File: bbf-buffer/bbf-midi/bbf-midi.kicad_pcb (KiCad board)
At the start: 4 copper layers, 31.8 x 52.1 mm, 17 parts, among them J1 Conn_02x05_Odd_Even, J2 Conn_02x05_Odd_Even, J3 DIN-5_180degree, J4 DIN-5_180degree, J5 Conn_01x03, U1 TLV1117-50, U2 6N137

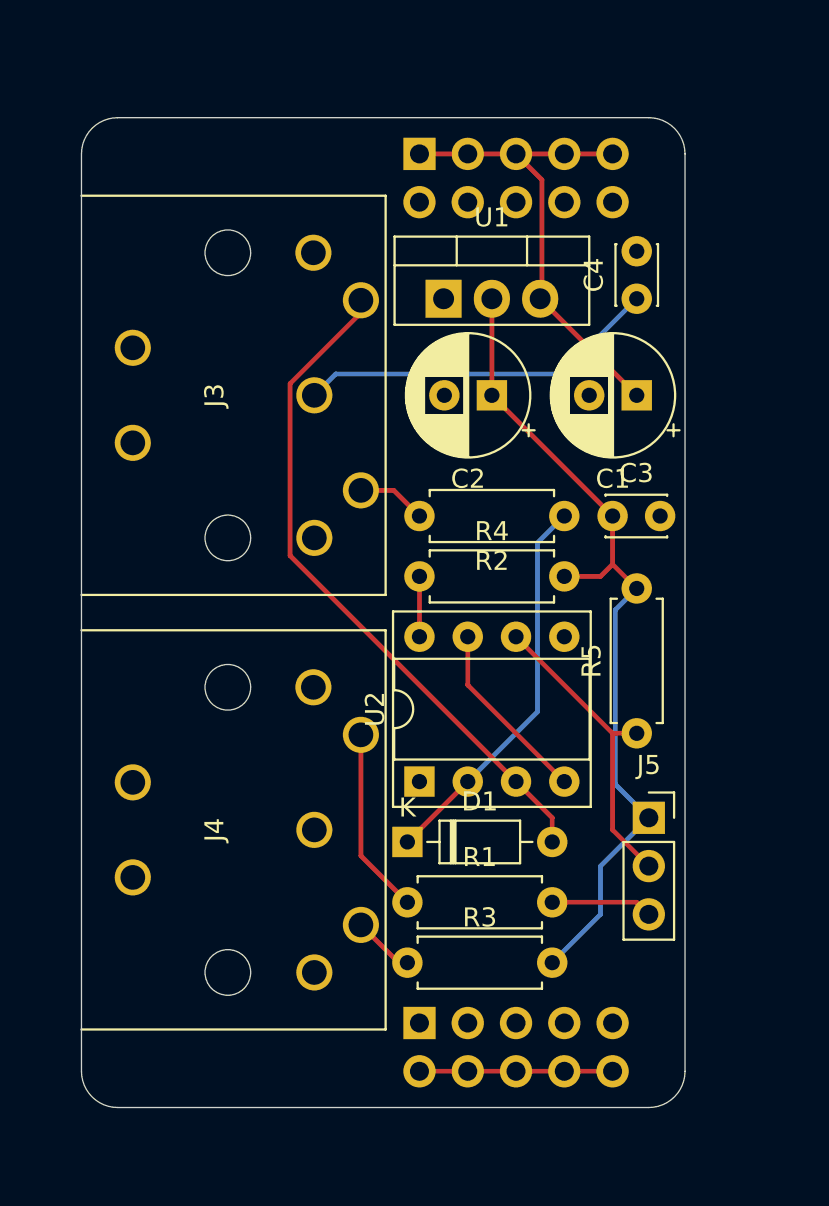
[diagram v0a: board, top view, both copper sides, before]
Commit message: Update midi friend to 3.3v, including RX buffer.
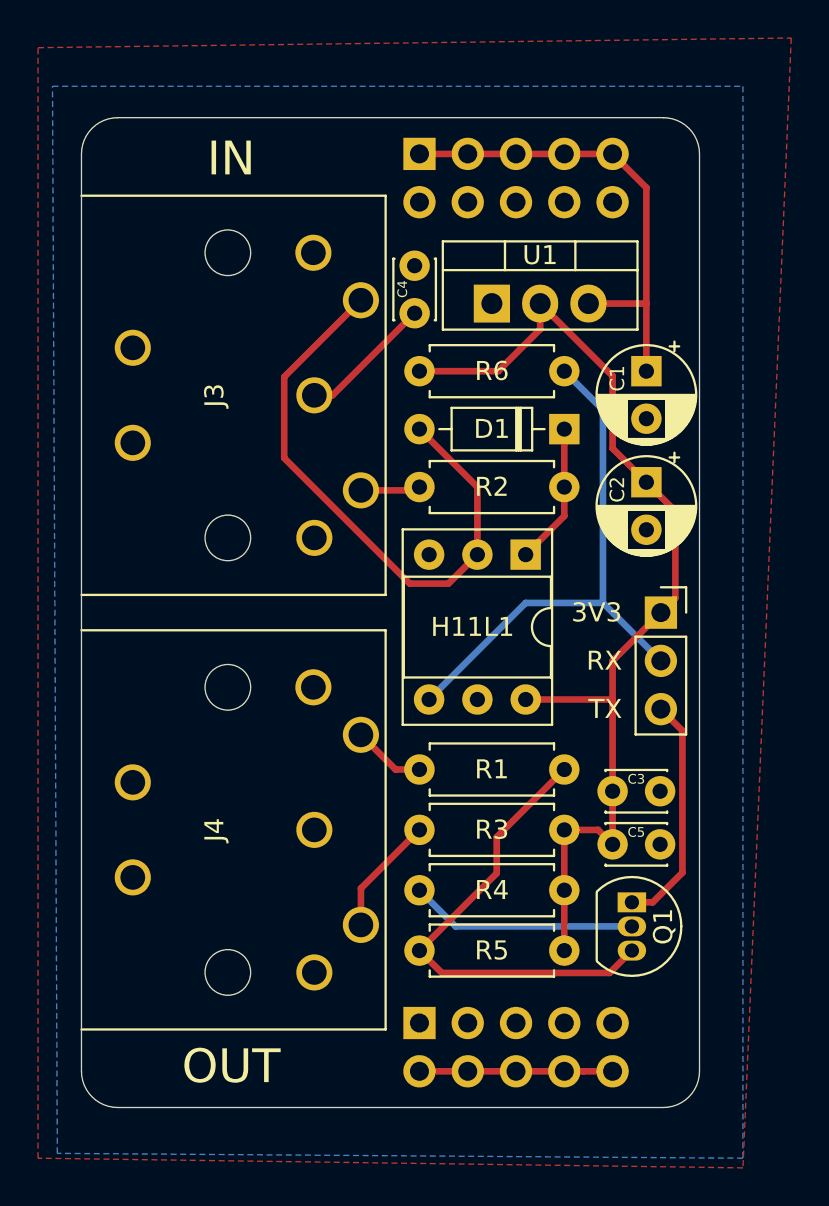
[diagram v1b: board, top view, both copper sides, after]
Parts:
- removed U2: 6N137, Package_DIP:DIP-8_W7.62mm_Socket
- added C5: 100n, Capacitor_THT:C_Disc_D3.0mm_W2.0mm_P2.50mm, F.Cu at (152.4, 125.2)
- added H11L1: H11L1, Package_DIP:DIP-6_W7.62mm_Socket, F.Cu at (147.8, 110.0)
- added Q1: 2N3904, Package_TO_SOT_THT:TO-92_Inline, F.Cu at (153.4, 128.3)
- added R5: 1K, Resistor_THT:R_Axial_DIN0207_L6.3mm_D2.5mm_P7.62mm_Horizontal, F.Cu at (142.2, 130.8)
- C1, C2: footprint Capacitor_THT:CP_Radial_D6.3mm_P2.50mm -> Capacitor_THT:CP_Radial_D5.0mm_P2.50mm
- R1: value 220 -> 33
- R3: value 220 -> 10
- U1: value TLV1117-50 -> TLV1117-33
- moved D1 23.2 mm to (149.9, 103.4), turned to 180 degrees
- moved R6 19.4 mm to (149.9, 100.3), turned to 180 degrees
- moved R4 16.5 mm to (142.2, 127.6)
- moved C3 14.5 mm to (152.4, 122.4)
- moved C4 11.7 mm to (142.0, 97.3)
- moved J5 10.8 mm to (154.9, 113.0)
- moved C2 9.33 mm to (154.2, 106.2), turned to 270 degrees
- moved R1 7.01 mm to (142.2, 121.3)
- moved R3 7.01 mm to (142.2, 124.5)
- moved U1 2.55 mm to (146.1, 96.8)
- moved R2 1.52 mm to (149.9, 106.4)
- moved C1 1.37 mm to (154.2, 100.3), turned to 270 degrees
- renumbered R5 to R6
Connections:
- R1 pad 2: Net-(J5-Pad3) -> Net-(Q1-Pad3)
- U1 pad 1: GND -> (no net)
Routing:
- net Net-(Q1-Pad3): track 0.00 -> 24.8 mm
- net Net-(D1-Pad1): track 20.6 -> 7.45 mm
- net Net-(J5-Pad2): track 16.2 -> 28.6 mm
- net Net-(C4-Pad1): track 19.1 -> 7.06 mm
- net VCC: track 44.2 -> 55.2 mm
- net (no net): track 9.72 -> 0.00 mm
- net Net-(Q1-Pad2): track 3.17 -> 12.0 mm
- net Net-(J5-Pad3): track 5.34 -> 12.4 mm
- net Net-(J4-Pad5): track 9.82 -> 3.84 mm
- net Net-(D1-Pad2): track 35.7 -> 31.4 mm
- net Net-(J4-Pad4): track 3.27 -> 6.28 mm
- added copper zone on B.Cu, net GND
- added copper zone on F.Cu, net GND
- removed copper zone on In1.Cu, net GND
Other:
- board size 31.8 x 52.1 mm -> 32.5 x 52.1 mm
- copper layers 4 -> 2
- board text added: "3V3"
- board text added: "IN"
- board text added: "OUT"
- board text added: "RX"
- board text added: "TX"
